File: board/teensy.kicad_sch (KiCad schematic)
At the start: 1 part, among them U2 Teensy4.1_DEV-16771

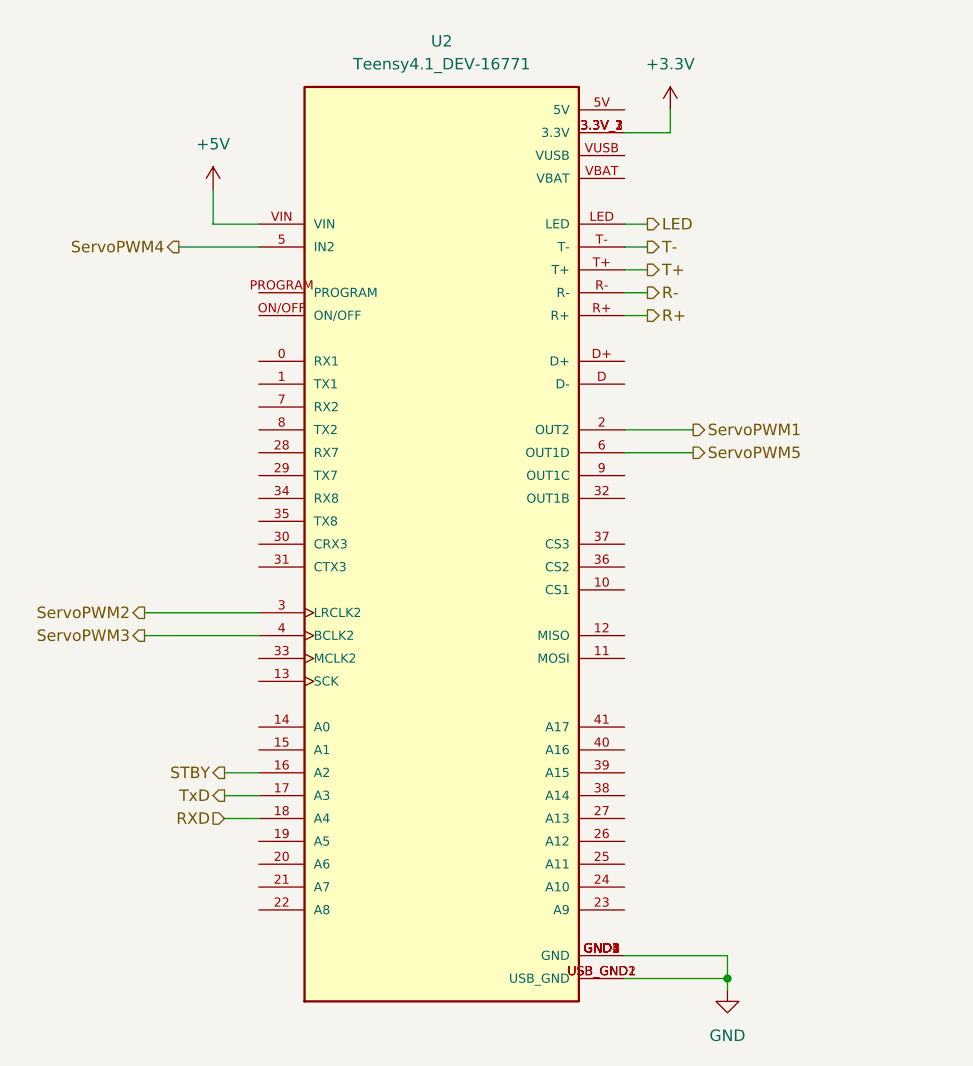
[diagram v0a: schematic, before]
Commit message: Added Servo, cleaned up schematic
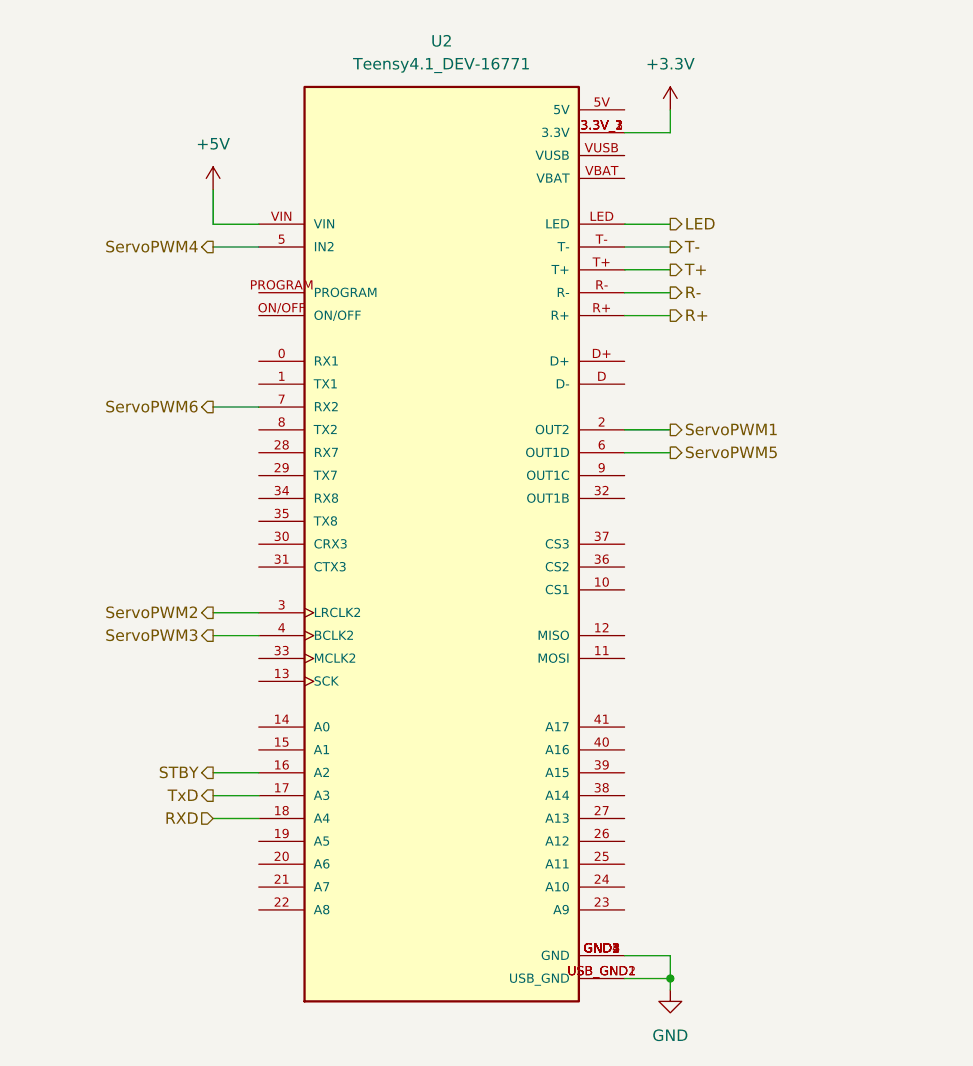
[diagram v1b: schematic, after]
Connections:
- net ServoPWM6: now reaches U2.7 (RX2)
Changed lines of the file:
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@@
 	(paper "A4")
 	(junction
-		(at 166.37 138.43)
+		(at 160.02 138.43)
 		(diameter 0)
 		(color 0 0 0 0)
@@
 	(wire
 		(pts
-			(xy 110.49 120.65) (xy 114.3 120.65)
-		)
-		(stroke
-			(width 0)
-			(type default)
-		)
-	)
-	(wire
-		(pts
-			(xy 154.94 77.47) (xy 162.56 77.47)
-		)
-		(stroke
-			(width 0)
-			(type default)
-		)
-	)
-	(wire
-		(pts
-			(xy 166.37 135.89) (xy 166.37 138.43)
-		)
-		(stroke
-			(width 0)
-			(type default)
-		)
-	)
-	(wire
-		(pts
-			(xy 154.94 64.77) (xy 157.48 64.77)
+			(xy 109.22 120.65) (xy 114.3 120.65)
+		)
+		(stroke
+			(width 0)
+			(type default)
+		)
+	)
+	(wire
+		(pts
+			(xy 154.94 77.47) (xy 160.02 77.47)
+		)
+		(stroke
+			(width 0)
+			(type default)
+		)
+	)
+	(wire
+		(pts
+			(xy 160.02 135.89) (xy 160.02 138.43)
+		)
+		(stroke
+			(width 0)
+			(type default)
+		)
+	)
+	(wire
+		(pts
+			(xy 154.94 64.77) (xy 160.02 64.77)
 		)
 		(stroke
@@
 	(wire
 		(pts
-			(xy 154.94 80.01) (xy 162.56 80.01)
-		)
-		(stroke
-			(width 0)
-			(type default)
-		)
-	)
-	(wire
-		(pts
-			(xy 166.37 138.43) (xy 166.37 139.7)
-		)
-		(stroke
-			(width 0)
-			(type default)
-		)
-	)
-	(wire
-		(pts
-			(xy 154.94 57.15) (xy 157.48 57.15)
-		)
-		(stroke
-			(width 0)
-			(type default)
-		)
-	)
-	(wire
-		(pts
-			(xy 154.94 135.89) (xy 166.37 135.89)
-		)
-		(stroke
-			(width 0)
-			(type default)
-		)
-	)
-	(wire
-		(pts
-			(xy 101.6 97.79) (xy 114.3 97.79)
-		)
-		(stroke
-			(width 0)
-			(type default)
-		)
-	)
-	(wire
-		(pts
-			(xy 154.94 62.23) (xy 157.48 62.23)
+			(xy 154.94 80.01) (xy 160.02 80.01)
+		)
+		(stroke
+			(width 0)
+			(type default)
+		)
+	)
+	(wire
+		(pts
+			(xy 160.02 138.43) (xy 160.02 139.7)
+		)
+		(stroke
+			(width 0)
+			(type default)
+		)
+	)
+	(wire
+		(pts
+			(xy 154.94 57.15) (xy 160.02 57.15)
+		)
+		(stroke
+			(width 0)
+			(type default)
+		)
+	)
+	(wire
+		(pts
+			(xy 154.94 135.89) (xy 160.02 135.89)
+		)
+		(stroke
+			(width 0)
+			(type default)
+		)
+	)
+	(wire
+		(pts
+			(xy 109.22 97.79) (xy 114.3 97.79)
+		)
+		(stroke
+			(width 0)
+			(type default)
+		)
+	)
+	(wire
+		(pts
+			(xy 154.94 62.23) (xy 160.02 62.23)
 		)
 		(stroke
@@
 	(wire
 		(pts
-			(xy 154.94 138.43) (xy 166.37 138.43)
-		)
-		(stroke
-			(width 0)
-			(type default)
-		)
-	)
-	(wire
-		(pts
-			(xy 105.41 57.15) (xy 114.3 57.15)
-		)
-		(stroke
-			(width 0)
-			(type default)
-		)
-	)
-	(wire
-		(pts
-			(xy 154.94 59.69) (xy 157.48 59.69)
+			(xy 154.94 138.43) (xy 160.02 138.43)
+		)
+		(stroke
+			(width 0)
+			(type default)
+		)
+	)
+	(wire
+		(pts
+			(xy 109.22 57.15) (xy 114.3 57.15)
+		)
+		(stroke
+			(width 0)
+			(type default)
+		)
+	)
+	(wire
+		(pts
+			(xy 154.94 59.69) (xy 160.02 59.69)
 		)
 		(stroke
@@
 	(wire
 		(pts
-			(xy 154.94 54.61) (xy 157.48 54.61)
-		)
-		(stroke
-			(width 0)
-			(type default)
-		)
-	)
-	(wire
-		(pts
-			(xy 101.6 100.33) (xy 114.3 100.33)
-		)
-		(stroke
-			(width 0)
-			(type default)
-		)
-	)
-	(wire
-		(pts
-			(xy 110.49 118.11) (xy 114.3 118.11)
-		)
-		(stroke
-			(width 0)
-			(type default)
-		)
-	)
-	(wire
-		(pts
-			(xy 110.49 115.57) (xy 114.3 115.57)
+			(xy 109.22 74.93) (xy 114.3 74.93)
+		)
+		(stroke
+			(width 0)
+			(type default)
+		)
+	)
+	(wire
+		(pts
+			(xy 154.94 54.61) (xy 160.02 54.61)
+		)
+		(stroke
+			(width 0)
+			(type default)
+		)
+	)
+	(wire
+		(pts
+			(xy 109.22 100.33) (xy 114.3 100.33)
+		)
+		(stroke
+			(width 0)
+			(type default)
+		)
+	)
+	(wire
+		(pts
+			(xy 109.22 118.11) (xy 114.3 118.11)
+		)
+		(stroke
+			(width 0)
+			(type default)
+		)
+	)
+	(wire
+		(pts
+			(xy 109.22 115.57) (xy 114.3 115.57)
 		)
 		(stroke
@@
 	(hierarchical_label "ServoPWM2"
 		(shape output)
-		(at 101.6 97.79 180)
+		(at 109.22 97.79 180)
+		(effects
+			(font
+				(size 1.27 1.27)
+			)
+			(justify right)
+		)
+	)
+	(hierarchical_label "ServoPWM6"
+		(shape output)
+		(at 109.22 74.93 180)
 		(effects
 			(font
@@
 	(hierarchical_label "R+"
 		(shape output)
-		(at 157.48 64.77 0)
+		(at 160.02 64.77 0)
 		(effects
 			(font
@@
 	(hierarchical_label "LED"
 		(shape output)
-		(at 157.48 54.61 0)
+		(at 160.02 54.61 0)
 		(effects
 			(font
@@
 	(hierarchical_label "ServoPWM1"
 		(shape output)
-		(at 162.56 77.47 0)
+		(at 160.02 77.47 0)
 		(effects
 			(font
@@
 	(hierarchical_label "ServoPWM4"
 		(shape output)
-		(at 105.41 57.15 180)
+		(at 109.22 57.15 180)
 		(effects
 			(font
@@
 	(hierarchical_label "T+"
 		(shape output)
-		(at 157.48 59.69 0)
+		(at 160.02 59.69 0)
 		(effects
 			(font
@@
 	(hierarchical_label "T-"
 		(shape output)
-		(at 157.48 57.15 0)
+		(at 160.02 57.15 0)
 		(effects
 			(font
@@
 	(hierarchical_label "TxD"
 		(shape output)
-		(at 110.49 118.11 180)
+		(at 109.22 118.11 180)
 		(effects
 			(font
@@
 	(hierarchical_label "ServoPWM5"
 		(shape output)
-		(at 162.56 80.01 0)
+		(at 160.02 80.01 0)
 		(effects
 			(font
@@
 	(hierarchical_label "STBY"
 		(shape output)
-		(at 110.49 115.57 180)
+		(at 109.22 115.57 180)
 		(effects
 			(font
@@
 	(hierarchical_label "ServoPWM3"
 		(shape output)
-		(at 101.6 100.33 180)
+		(at 109.22 100.33 180)
 		(effects
 			(font
@@
 	(hierarchical_label "RXD"
 		(shape input)
-		(at 110.49 120.65 180)
+		(at 109.22 120.65 180)
 		(effects
 			(font
@@
 	(hierarchical_label "R-"
 		(shape output)
-		(at 157.48 62.23 0)
+		(at 160.02 62.23 0)
 		(effects
 			(font
@@
 	(symbol
 		(lib_id "power:GND")
-		(at 166.37 139.7 0)
+		(at 160.02 139.7 0)
 		(unit 1)
 		(exclude_from_sim no)
@@
 		(fields_autoplaced yes)
 		(property "Reference" "#PWR08"
-			(at 166.37 146.05 0)
+			(at 160.02 146.05 0)
 			(effects
 				(font
@@
 		)
 		(property "Value" "GND"
-			(at 166.37 144.78 0)
+			(at 160.02 144.78 0)
 			(effects
 				(font
@@
 		)
 		(property "Footprint" ""
-			(at 166.37 139.7 0)
+			(at 160.02 139.7 0)
 			(effects
 				(font
@@
 		)
 		(property "Datasheet" ""
-			(at 166.37 139.7 0)
+			(at 160.02 139.7 0)
 			(effects
 				(font
@@
 		)
 		(property "Description" "Power symbol creates a global label with name \"GND\" , ground"
-			(at 166.37 139.7 0)
-			(effects
-				(font
+			(at 160.02 139.7 0)
+			(effects
+				(font

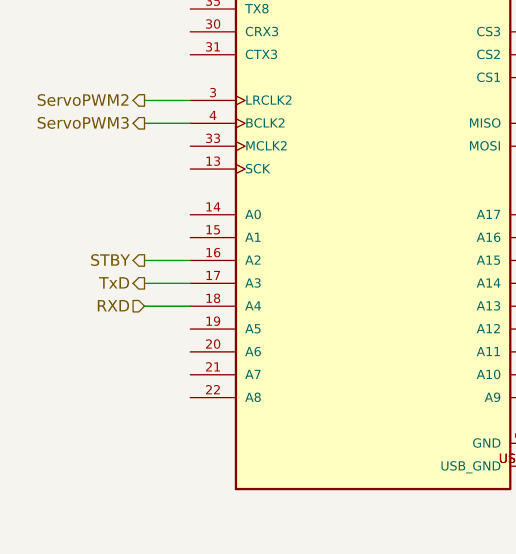
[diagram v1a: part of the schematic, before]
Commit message: Moved things to make more sense
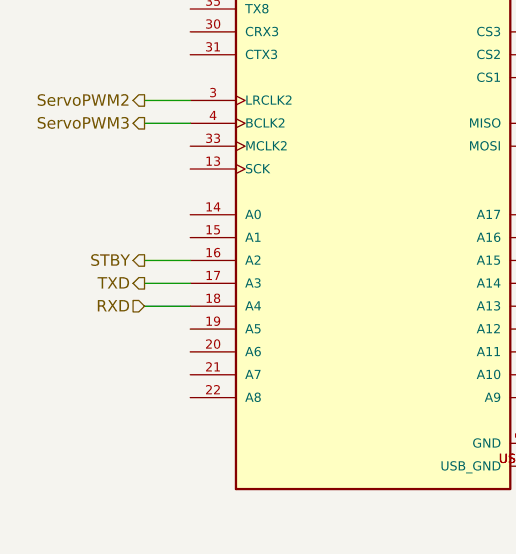
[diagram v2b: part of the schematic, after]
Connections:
- net TxD renamed TXD
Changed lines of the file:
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@@
 		)
 	)
-	(hierarchical_label "TxD"
+	(hierarchical_label "TXD"
 		(shape output)
 		(at 109.22 118.11 180)

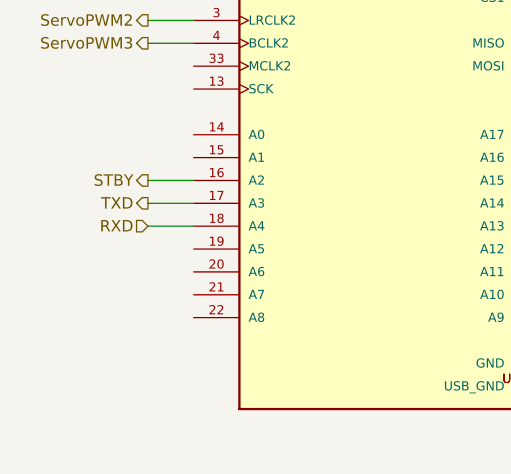
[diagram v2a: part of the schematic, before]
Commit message: Added Parts, Renamed Parts
Added in switches, buttons, & multiple anderson connections for power.
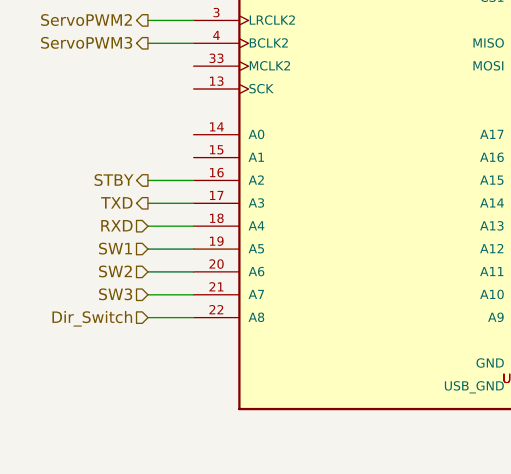
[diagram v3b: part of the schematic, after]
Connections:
- net SW1: now reaches U2.19 (A5)
- net SW2: now reaches U2.20 (A6)
- net SW3: now reaches U2.21 (A7)
- net Dir_Switch: now reaches U2.22 (A8)
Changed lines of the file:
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@@
+	(wire
+		(pts
+			(xy 109.22 128.27) (xy 114.3 128.27)
+		)
+		(stroke
+			(width 0)
+			(type default)
+		)
+	)
 	(wire
 		(pts
@@
 	(wire
 		(pts
+			(xy 109.22 123.19) (xy 114.3 123.19)
+		)
+		(stroke
+			(width 0)
+			(type default)
+		)
+	)
+	(wire
+		(pts
 			(xy 109.22 54.61) (xy 114.3 54.61)
 		)
@@
 	(wire
 		(pts
+			(xy 109.22 125.73) (xy 114.3 125.73)
+		)
+		(stroke
+			(width 0)
+			(type default)
+		)
+	)
+	(wire
+		(pts
 			(xy 154.94 57.15) (xy 160.02 57.15)
 		)
@@
 		)
 	)
+	(wire
+		(pts
+			(xy 109.22 130.81) (xy 114.3 130.81)
+		)
+		(stroke
+			(width 0)
+			(type default)
+		)
+	)
+	(hierarchical_label "SW3"
+		(shape input)
+		(at 109.22 128.27 180)
+		(effects
+			(font
+				(size 1.27 1.27)
+			)
+			(justify right)
+		)
+	)
 	(hierarchical_label "ServoPWM2"
 		(shape output)
@@
 		)
 	)
+	(hierarchical_label "SW1"
+		(shape input)
+		(at 109.22 123.19 180)
+		(effects
+			(font
+				(size 1.27 1.27)
+			)
+			(justify right)
+		)
+	)
 	(hierarchical_label "ServoPWM1"
 		(shape output)
@@
 		)
 	)
+	(hierarchical_label "Dir_Switch"
+		(shape input)
+		(at 109.22 130.81 180)
+		(effects
+			(font
+				(size 1.27 1.27)
+			)
+			(justify right)
+		)
+	)
 	(hierarchical_label "T+"
 		(shape output)
@@
 		)
 	)
+	(hierarchical_label "SW2"
+		(shape input)
+		(at 109.22 125.73 180)
+		(effects
+			(font
+				(size 1.27 1.27)
+			)
+			(justify right)
+		)
+	)

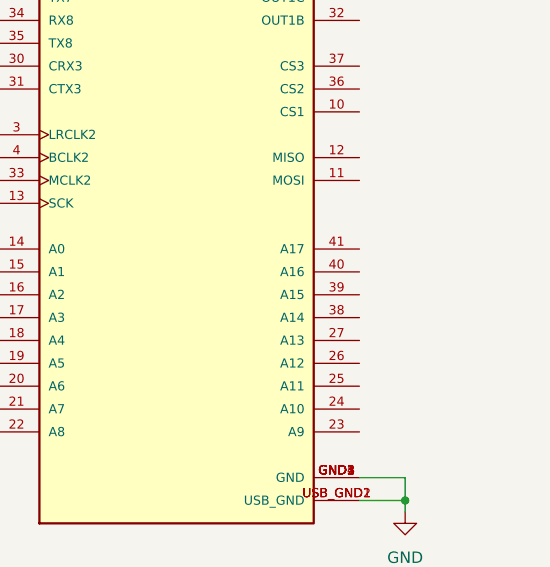
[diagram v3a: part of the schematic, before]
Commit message: added NPK and soil sensors pt. 1
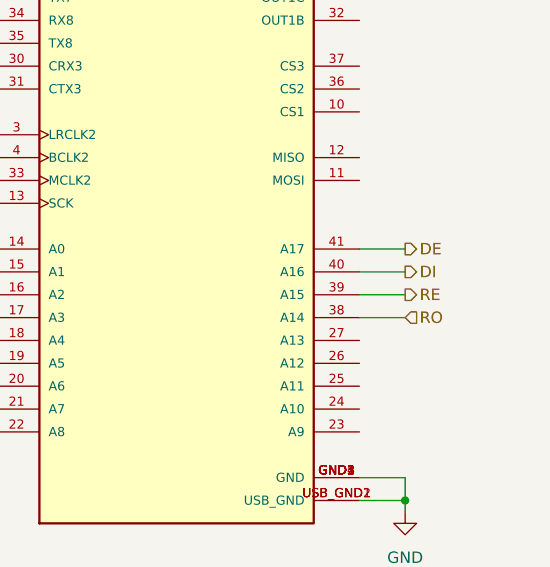
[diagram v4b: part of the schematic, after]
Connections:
- net RO: now reaches U2.38 (A14)
- net RE: now reaches U2.39 (A15)
- net DI: now reaches U2.40 (A16)
- net DE: now reaches U2.41 (A17)
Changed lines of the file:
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@@
+	(wire
+		(pts
+			(xy 154.94 110.49) (xy 160.02 110.49)
+		)
+		(stroke
+			(width 0)
+			(type default)
+		)
+	)
 	(wire
 		(pts
@@
 	(wire
 		(pts
+			(xy 154.94 118.11) (xy 160.02 118.11)
+		)
+		(stroke
+			(width 0)
+			(type default)
+		)
+	)
+	(wire
+		(pts
 			(xy 154.94 77.47) (xy 160.02 77.47)
 		)
@@
 		(pts
 			(xy 109.22 74.93) (xy 114.3 74.93)
+		)
+		(stroke
+			(width 0)
+			(type default)
+		)
+	)
+	(wire
+		(pts
+			(xy 154.94 113.03) (xy 160.02 113.03)
+		)
+		(stroke
+			(width 0)
+			(type default)
+		)
+	)
+	(wire
+		(pts
+			(xy 154.94 115.57) (xy 160.02 115.57)
 		)
 		(stroke
@@
 		)
 	)
+	(hierarchical_label "RE"
+		(shape output)
+		(at 160.02 115.57 0)
+		(effects
+			(font
+				(size 1.27 1.27)
+			)
+			(justify left)
+		)
+	)
 	(hierarchical_label "ServoPWM2"
 		(shape output)
@@
 			)
 			(justify right)
+		)
+	)
+	(hierarchical_label "DE"
+		(shape output)
+		(at 160.02 110.49 0)
+		(effects
+			(font
+				(size 1.27 1.27)
+			)
+			(justify left)
 		)
 	)
@@
 		)
 	)
+	(hierarchical_label "RO"
+		(shape input)
+		(at 160.02 118.11 0)
+		(effects
+			(font
+				(size 1.27 1.27)
+			)
+			(justify left)
+		)
+	)
 	(hierarchical_label "ServoPWM5"
 		(shape output)
@@
 		)
 	)
+	(hierarchical_label "DI"
+		(shape output)
+		(at 160.02 113.03 0)
+		(effects
+			(font
+				(size 1.27 1.27)
+			)
+			(justify left)
+		)
+	)

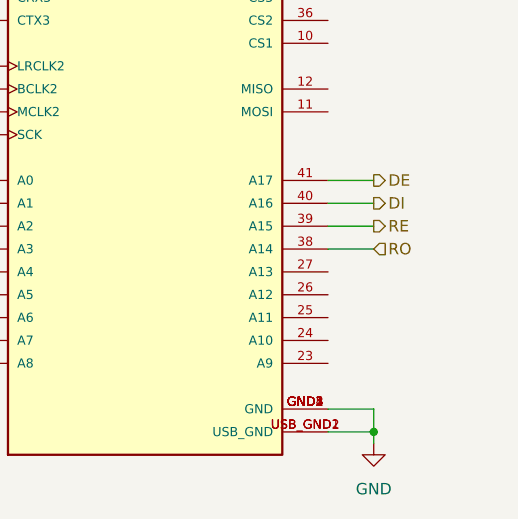
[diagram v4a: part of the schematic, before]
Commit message: Soil sensors pt. 2
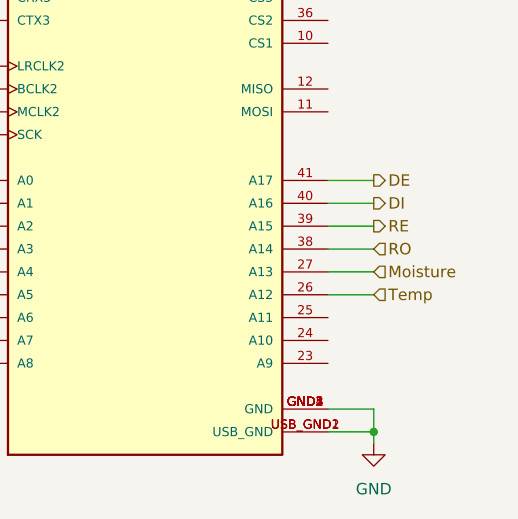
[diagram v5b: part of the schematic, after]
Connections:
- net Temp: now reaches U2.26 (A12)
- net Moisture: now reaches U2.27 (A13)
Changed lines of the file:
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@@
+	(wire
+		(pts
+			(xy 154.94 120.65) (xy 160.02 120.65)
+		)
+		(stroke
+			(width 0)
+			(type default)
+		)
+	)
 	(wire
 		(pts
@@
 	(wire
 		(pts
+			(xy 154.94 123.19) (xy 160.02 123.19)
+		)
+		(stroke
+			(width 0)
+			(type default)
+		)
+	)
+	(wire
+		(pts
 			(xy 109.22 115.57) (xy 114.3 115.57)
 		)
@@
 		)
 	)
+	(hierarchical_label "Moisture"
+		(shape input)
+		(at 160.02 120.65 0)
+		(effects
+			(font
+				(size 1.27 1.27)
+			)
+			(justify left)
+		)
+	)
 	(hierarchical_label "RE"
 		(shape output)
@@
 		)
 	)
+	(hierarchical_label "Temp"
+		(shape input)
+		(at 160.02 123.19 0)
+		(effects
+			(font
+				(size 1.27 1.27)
+			)
+			(justify left)
+		)
+	)
